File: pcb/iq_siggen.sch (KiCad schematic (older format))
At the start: 57 parts

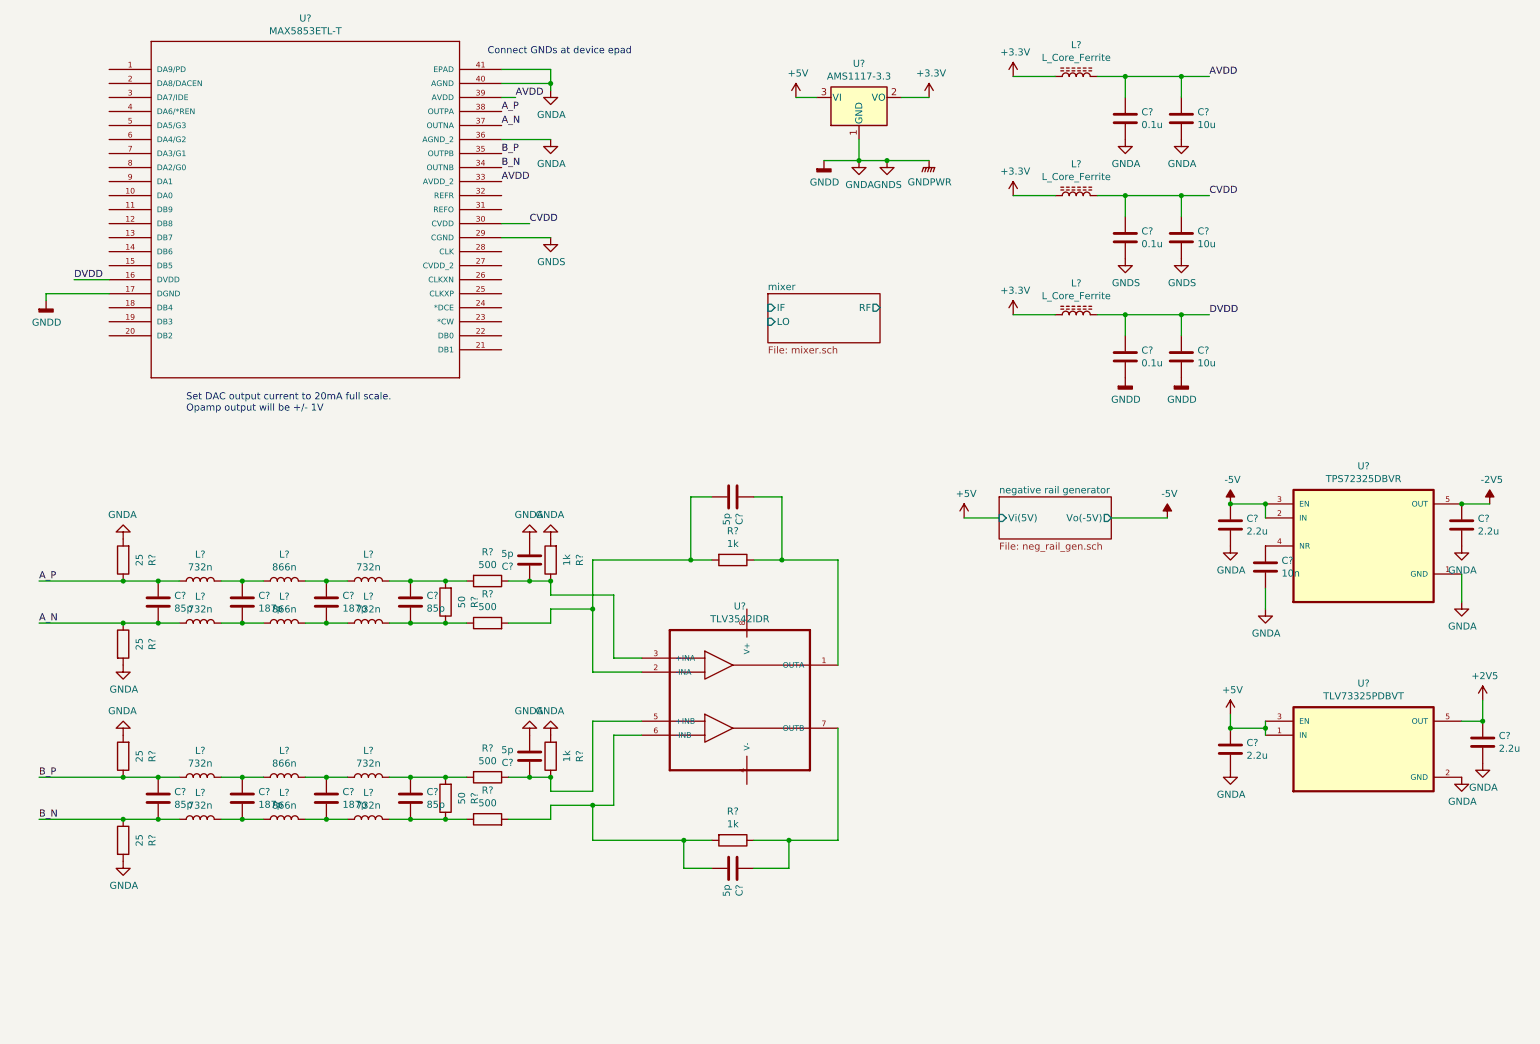
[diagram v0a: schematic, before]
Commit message: Define pin map, clean up schematic
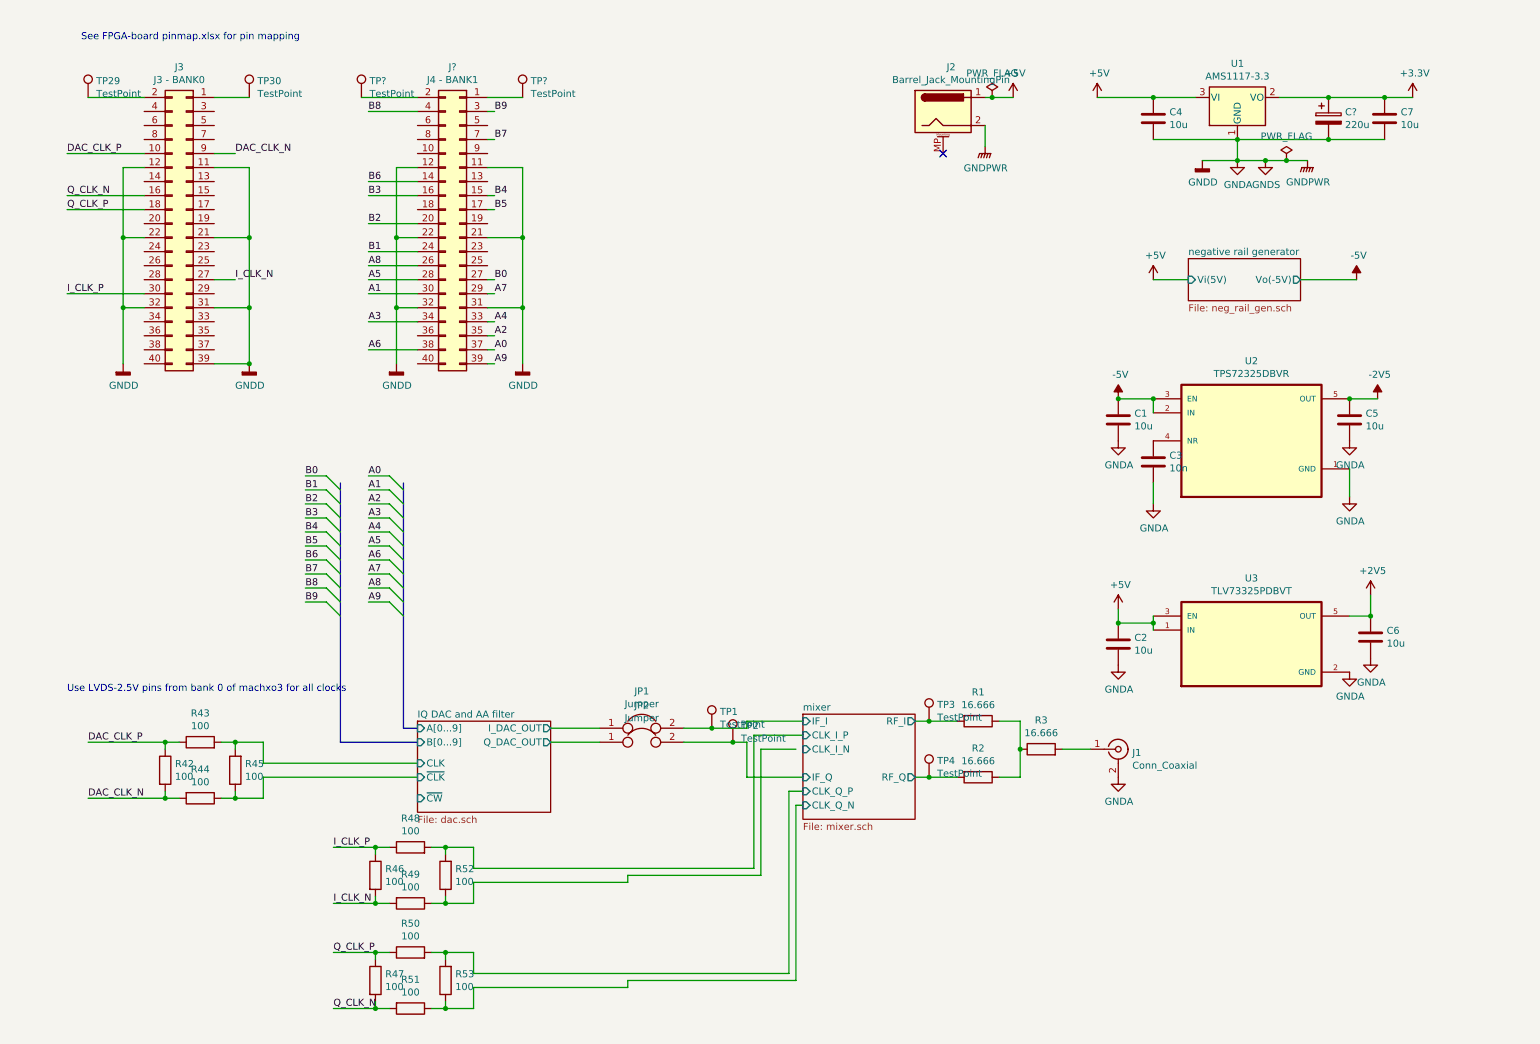
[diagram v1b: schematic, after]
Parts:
- removed C? (x3): 0.1u, symbol Device:C
- removed C? (x3): 10u, symbol Device:C
- removed C? (x4): 85p, symbol Device:C
- removed C? (x4): 187p, symbol Device:C
- removed C? (x4): 5p, symbol Device:C
- removed L? (x3): L_Core_Ferrite, symbol Device:L_Core_Ferrite
- removed L? (x8): 732n, symbol Device:L
- removed L? (x4): 866n, symbol Device:L
- removed R? (x4): 25, symbol Device:R
- removed R? (x4): 500, symbol Device:R
- removed R? (x4): 1k, symbol Device:R
- removed R? (x2): 50, symbol Device:R
- removed U?: MAX5853ETL-T, 21-0141I_T4066-2, symbol MAX5853ETL-T:MAX5853ETL-T
- removed U?: TLV3542IDR, SOIC127P599X175-8N, symbol TLV3542IDR:TLV3542IDR
- added C4, C7: 10u, symbol Device:C
- added C?: 220u, symbol Device:CP
- added J1: Conn_Coaxial, symbol Connector:Conn_Coaxial
- added J2: Barrel_Jack_MountingPin, symbol Connector:Barrel_Jack_MountingPin
- added J3: J3 - BANK0, symbol Connector_Generic:Conn_02x20_Odd_Even
- added J?: J4 - BANK1, symbol Connector_Generic:Conn_02x20_Odd_Even
- added JP1, JP2: Jumper, symbol Device:Jumper
- added R1, R2, R3: 16.666, symbol Device:R
- added R42, R43, R44, R45, R46, R47, R48, R49, R50, R51, R52, R53: 100, symbol Device:R
- added TP1, TP2, TP29, TP3, TP30, TP4, TP? (x2): TestPoint, symbol Connector:TestPoint
- C1, C2, C5, C6: renamed from C?; value 2.2u -> 10u
- gave numbers to parts that had none: 4
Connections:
- net +3V3: now also C7.1, C?.1
- net +5V: now also C4.1, J2.1
- net GNDA: now also C4.2, C7.2, C?.2, J1.2 (Ext), J2.2, J3.11 (Pin_11), J3.12 (Pin_12), J3.21 (Pin_21), J3.22 (Pin_22), J3.31 (Pin_31), J3.32 (Pin_32), J3.39 (Pin_39), J?.11 (Pin_11), J?.12 (Pin_12), J?.21 (Pin_21), J?.22 (Pin_22), J?.31 (Pin_31), J?.32 (Pin_32)
- new net: J1.1 (In), R3.2
- new net: R1.1, R2.1, R3.1
- new net: J3.1 (Pin_1), TP30.1
- new net: J3.2 (Pin_2), TP29.1
- new net: R49.1, R52.1
- new net: J?.1 (Pin_1), TP?.1
- new net: J?.2 (Pin_2), TP?.1
- new net A0: J?.37 (Pin_37)
- new net A1: J?.30 (Pin_30)
- new net A2: J?.35 (Pin_35)
- new net A3: J?.34 (Pin_34)
- new net A4: J?.33 (Pin_33)
- new net A5: J?.28 (Pin_28)
- new net A6: J?.38 (Pin_38)
- new net A7: J?.29 (Pin_29)
- new net A8: J?.26 (Pin_26)
- new net A9: J?.39 (Pin_39)
- new net B0: J?.27 (Pin_27)
- new net B1: J?.24 (Pin_24)
- new net B2: J?.20 (Pin_20)
- new net B3: J?.16 (Pin_16)
- new net B4: J?.15 (Pin_15)
- new net B5: J?.17 (Pin_17)
- new net B6: J?.14 (Pin_14)
- new net B7: J?.7 (Pin_7)
- new net B8: J?.4 (Pin_4)
- new net B9: J?.3 (Pin_3)
- new net DAC_CLK_N: J3.9 (Pin_9), R42.2, R44.2
- new net DAC_CLK_P: J3.10 (Pin_10), R42.1, R43.1
- new net IQ DAC and AA filter/CLK: R43.2, R45.2
- new net IQ DAC and AA filter/I_DAC_OUT: JP1.1
- new net IQ DAC and AA filter/Q_DAC_OUT: JP2.1
- new net IQ DAC and AA filter/~CLK: R44.1, R45.1
- new net I_CLK_N: J3.27 (Pin_27), R46.2, R49.2
- new net I_CLK_P: J3.30 (Pin_30), R46.1, R48.1
- new net Q_CLK_N: J3.16 (Pin_16), R47.2, R51.2
- new net Q_CLK_P: J3.18 (Pin_18), R47.1, R50.1
- new net mixer/CLK_I_P: R48.2, R52.2
- new net mixer/CLK_Q_N: R51.1, R53.1
- new net mixer/CLK_Q_P: R50.2, R53.2
- new net mixer/IF_I: JP1.2, TP1.1
- new net mixer/IF_Q: JP2.2, TP2.1
- new net mixer/RF_I: R1.2, TP3.1
- new net mixer/RF_Q: R2.2, TP4.1
- no-connect marks 0 -> 1
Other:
- note added: "See FPGA-board pinmap.xlsx for pin mapping"
- note added: "Use LVDS-2.5V pins from bank 0 of machxo3 for all clocks"
- note removed: "Connect GNDs at device epad"
- note removed: "Set DAC output current to 20mA full scale.\nOpamp output will be +/- 1V"
- moved on the sheet: C1, C2, C3, C5, C6, U1, U2, U3

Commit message: clean up ERC, more DFT stuff, started sigma delta adc
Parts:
- removed JP1, JP2: Jumper, symbol Device:Jumper
- added C64: 3p, symbol Device:C
- added D12, D13, D14, D15: LED, symbol Device:LED
- added J10, J11, J12, J13, J14, J17, J8: Conn_01x01_Male, symbol Connector:Conn_01x01_Male
- added J15, J16, J5, J6: Conn_Coaxial, symbol Connector:Conn_Coaxial
- added J7, J9: Conn_01x10_Male, symbol Connector:Conn_01x10_Male
- added JP1, JP2: SolderJumper_3_Open, symbol Jumper:SolderJumper_3_Open
- added JP11: Jumper, symbol Device:Jumper
- added R100, R101, R89, R90, R91: DNI-50, symbol Device:R
- added R102, R103, R104, R105: 220, symbol Device:R
- added R54, R55, R56, R57, R58, R59: 0, symbol Device:R
- added R60, R61, R62, R63, R64, R65, R66, R67, R68, R69, R70, R71, R72, R73, R74, R75, R76, R77, R78, R79, R80, R81, R82, R83, R84, R92, R93, R94, R95, R96, R97: 22, symbol Device:R
- added R85, R86, R87, R88: 10k, symbol Device:R
- added SW1, SW2, SW3, SW4: SW_Push, symbol Switch:SW_Push
- added TP33, TP34, TP35, TP36, TP37, TP38, TP39, TP40, TP41, TP42, TP43, TP44, TP45, TP46, TP47, TP48, TP49: TestPoint, symbol Connector:TestPoint
- gave numbers to parts that had none: 4
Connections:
- net +2V5: now also TP49.1
- net +3V3: now also TP47.1
- net +5V: now also TP41.1, TP42.1
- net -2V5: now also TP48.1
- net -5V: now also TP43.1
- net A0: now also J9.1 (Pin_1), R83.2; no longer J4.37 (Pin_37)
- net A1: now also J9.2 (Pin_2), R70.1; no longer J4.30 (Pin_30)
- net A2: now also J9.3 (Pin_3), R82.2; no longer J4.35 (Pin_35)
- net A3: now also J9.4 (Pin_4), R71.1; no longer J4.34 (Pin_34)
- net A4: now also J9.5 (Pin_5), R81.2; no longer J4.33 (Pin_33)
- net A5: now also J9.6 (Pin_6), R69.1; no longer J4.28 (Pin_28)
- net A6: now also J9.7 (Pin_7), R72.1; no longer J4.38 (Pin_38)
- net A7: now also J9.8 (Pin_8), R80.2; no longer J4.29 (Pin_29)
- net A8: now also J9.9 (Pin_9), R68.1; no longer J4.26 (Pin_26)
- net A9: now also J9.10 (Pin_10), R84.2; no longer J4.39 (Pin_39)
- net B0: now also J7.1 (Pin_1), R79.2; no longer J4.27 (Pin_27)
- net B1: now also J7.2 (Pin_2), R67.1; no longer J4.24 (Pin_24)
- net B2: now also J7.3 (Pin_3), R66.1; no longer J4.20 (Pin_20)
- net B3: now also J7.4 (Pin_4), R65.1; no longer J4.16 (Pin_16)
- net B4: now also J7.5 (Pin_5), R76.2; no longer J4.15 (Pin_15)
- net B5: now also J7.6 (Pin_6), R77.2; no longer J4.17 (Pin_17)
- net B6: now also J7.7 (Pin_7), R64.1; no longer J4.14 (Pin_14)
- net B7: now also J7.8 (Pin_8), R75.2; no longer J4.7 (Pin_7)
- net B8: now also J7.9 (Pin_9), R60.1; no longer J4.4 (Pin_4)
- net B9: now also J7.10 (Pin_10), R73.2; no longer J4.3 (Pin_3)
- net DAC_CLK_N: now also R58.2, TP34.1; no longer J3.9 (Pin_9)
- net DAC_CLK_P: now also R54.1, TP33.1; no longer J3.10 (Pin_10)
- net GNDA: now also C64.2, D12.1 (K), D13.1 (K), D14.1 (K), D15.1 (K), J10.1 (Pin_1), J11.1 (Pin_1), J12.1 (Pin_1), J13.1 (Pin_1), J14.1 (Pin_1), J15.2 (Ext), J16.2 (Ext), J17.1 (Pin_1), J5.2 (Ext), J6.2 (Ext), R100.2, R101.2, R78.2, R85.1, R86.1, R87.1, R88.1, R89.2, R90.2, R91.2, R92.2, R95.2, R96.2, TP44.1, TP45.1, TP46.1
- net IQ DAC and AA filter/I_DAC_OUT: now also JP1.2 (C), R100.1
- net IQ DAC and AA filter/Q_DAC_OUT: now also JP2.2 (C), R101.1
- net I_CLK_N: now also R59.2, TP37.1; no longer J3.27 (Pin_27)
- net I_CLK_P: now also R57.1, TP36.1; no longer J3.30 (Pin_30)
- net Q_CLK_N: now also R55.1, TP39.1; no longer J3.16 (Pin_16)
- net Q_CLK_P: now also R56.1, TP38.1; no longer J3.18 (Pin_18)
- net mixer/IF_I: now also JP1.1 (A)
- net mixer/IF_Q: now also JP2.1 (A)
- net mixer/RF_I: now also R90.1
- net mixer/RF_Q: now also R89.1
- net RF_LP_FILTERED_OUT: now reaches J1.1 (In)
- net RF_LP_FILTERED_OUT: now also C64.1, JP11.2; no longer R3.2
- net VCCIO0: now reaches J3.1 (Pin_1), TP30.1
- net VCCIO0: now also J3.2 (Pin_2), TP29.1
- net LED0: now reaches J3.13 (Pin_13)
- net LED0: now also R102.1
- net LED1: now reaches J3.15 (Pin_15)
- net LED1: now also R103.1
- net LED2: now reaches J3.17 (Pin_17)
- net LED2: now also R104.1
- net LED3: now reaches J3.19 (Pin_19)
- net LED3: now also R105.1
- net VCCIO1: now reaches J4.1 (Pin_1), TP32.1
- net VCCIO1: now also J4.2 (Pin_2), TP31.1, SW1.2, SW2.2, SW3.2, SW4.2
- net at J4.10 (Pin_10): now also R63.2
- net CLK_OUT: now reaches J4.19 (Pin_19)
- net CLK_OUT: now also R92.1, R94.1
- net CLK_EXT_IN: now reaches J4.25 (Pin_25)
- net CLK_EXT_IN: now also R78.1, R93.1
- net at J4.5 (Pin_5): now also R74.1
- net at J4.6 (Pin_6): now also R61.2
- net at J4.8 (Pin_8): now also R62.2
- net at J4.9 (Pin_9): now also R97.1
- new net: J3.10 (Pin_10), R54.2
- new net: J3.16 (Pin_16), R55.2
- new net: J3.18 (Pin_18), R56.2
- new net: J3.27 (Pin_27), R59.1
- new net: J3.30 (Pin_30), R57.2
- new net: J3.9 (Pin_9), R58.1
- new net: J4.14 (Pin_14), R64.2
- new net: J4.15 (Pin_15), R76.1
- new net: J4.16 (Pin_16), R65.2
- new net: J4.17 (Pin_17), R77.1
- new net: J4.20 (Pin_20), R66.2
- new net: J4.24 (Pin_24), R67.2
- new net: J4.26 (Pin_26), R68.2
- new net: J4.27 (Pin_27), R79.1
- new net: J4.28 (Pin_28), R69.2
- new net: J4.29 (Pin_29), R80.1
- new net: J4.3 (Pin_3), R73.1
- new net: J4.30 (Pin_30), R70.2
- new net: J4.33 (Pin_33), R81.1
- new net: J4.34 (Pin_34), R71.2
- new net: J4.35 (Pin_35), R82.1
- new net: J4.37 (Pin_37), R83.1
- new net: J4.38 (Pin_38), R72.2
- new net: J4.39 (Pin_39), R84.1
- new net: J4.4 (Pin_4), R60.2
- new net: J4.7 (Pin_7), R75.1
- new net: J5.1 (In), R93.2, R95.1
- new net: J6.1 (In), R94.2, R96.1
- new net: D15.2 (A), R105.2
- new net: D12.2 (A), R102.2
- new net: D13.2 (A), R103.2
- new net: D14.2 (A), R104.2
- new net I_OUT: J15.1 (In), JP1.3 (B)
- new net Q_OUT: J16.1 (In), JP2.3 (B)
- new net RF_OUT: JP11.1, R3.2, R91.1, TP40.1
- new net SW0: R61.1, R85.2, SW1.1
- new net SW1: R62.1, R86.2, SW2.1
- new net SW2: R63.1, R87.2, SW3.1
- new net SW3: R74.2, R88.2, SW4.1
- new net ~CW: J8.1 (Pin_1), R97.2, TP35.1
- no-connect marks 1 -> 27
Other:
- moved on the sheet: C1, C2, C3, C4, C5, C6, C63, C7, J1, J2, J4, R42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

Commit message: started assigning footprints
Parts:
- C1, C2, C3, C4, C5, C6, C64, C7: footprint (none) -> Capacitor_SMD:C_0805_2012Metric_Pad1.15x1.40mm_HandSolder
- C63: footprint (none) -> Capacitor_Tantalum_SMD:CP_EIA-7343-20_Kemet-V_Pad2.25x2.55mm_HandSolder
- D12, D13, D14, D15: footprint (none) -> LED_SMD:LED_0805_2012Metric_Pad1.15x1.40mm_HandSolder
- R1, R100, R101, R102, R103, R104, R105, R2, R3, R42, R43, R44, R45, R46, R47, R48, R49, R50, R51, R52, R53, R54, R55, R56, R57, R58, R59, R60, R61, R62, R63, R64, R65, R66, R67, R68, R69, R70, R71, R72, R73, R74, R75, R76, R77, R78, R79, R80, R81, R82, R83, R84, R85, R86, R87, R88, R89, R90, R91, R92, R93, R94, R95, R96, R97: footprint (none) -> Resistor_SMD:R_0805_2012Metric_Pad1.20x1.40mm_HandSolder
- U2, U3: footprint SOT95P280X145-5N -> (none)
